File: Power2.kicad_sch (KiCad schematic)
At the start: 22 parts, among them U1001 AP64060QWU, U1002 AP7383, U1003 LM2776, U1004 XC6901D121MR-G

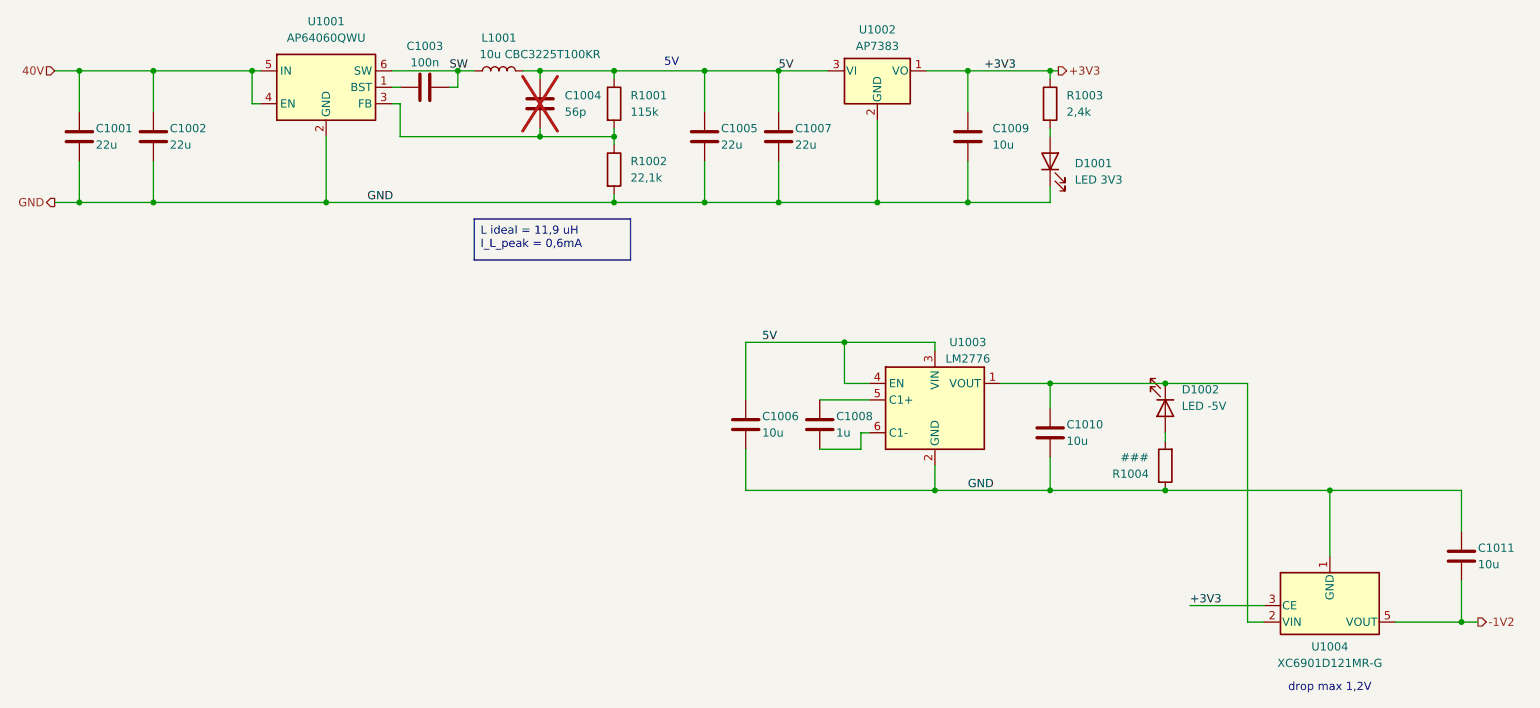
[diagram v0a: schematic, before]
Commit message: added Ch2 and removed global power flags
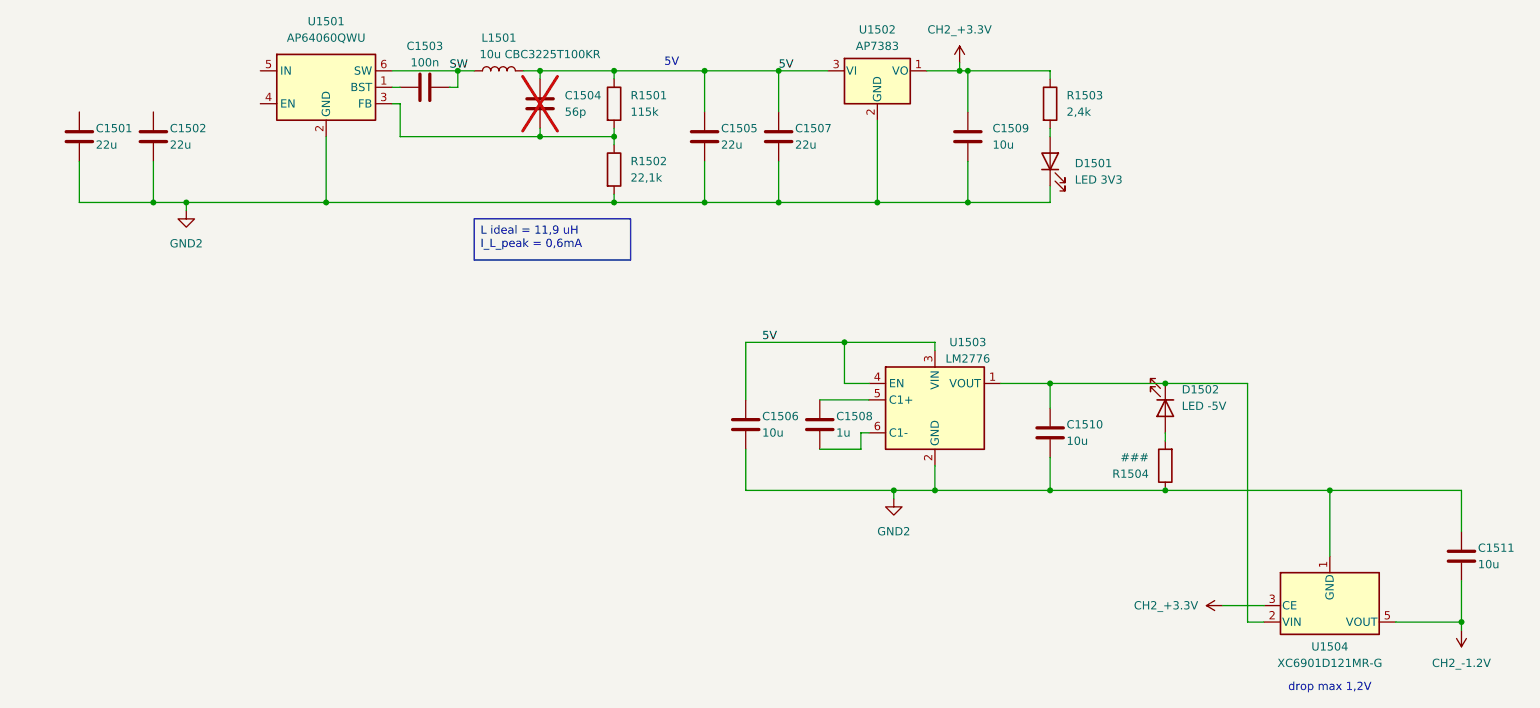
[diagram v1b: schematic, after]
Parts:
- removed C1001, C1002: 22u, Capacitor_SMD:C_1206_3216Metric, symbol Device:C
- removed C1003: 100n, Capacitor_SMD:C_0603_1608Metric, symbol Device:C
- removed C1004: 56p, Capacitor_SMD:C_0603_1608Metric, symbol Device:C
- removed C1005, C1007: 22u, Capacitor_SMD:C_0805_2012Metric, symbol Device:C
- removed C1006, C1009, C1010, C1011: 10u, Capacitor_SMD:C_0805_2012Metric, symbol Device:C
- removed C1008: 1u, Capacitor_SMD:C_0805_2012Metric, symbol Device:C
- removed D1001: LED 3V3, LED_SMD:LED_0603_1608Metric, symbol Device:LED
- removed D1002: LED -5V, LED_SMD:LED_0603_1608Metric, symbol Device:LED
- removed L1001: 10u CBC3225T100KR, Inductor_SMD:L_1210_3225Metric, symbol Device:L
- removed R1001: 115k, Resistor_SMD:R_0603_1608Metric, symbol Device:R
- removed R1002: 22,1k, Resistor_SMD:R_0603_1608Metric, symbol Device:R
- removed R1003: 2,4k, Resistor_SMD:R_0603_1608Metric, symbol Device:R
- removed R1004: ###, Resistor_SMD:R_0603_1608Metric, symbol Device:R
- removed U1001: AP64060QWU, Package_TO_SOT_SMD:TSOT-23-6, symbol Regulator_Switching:AP63200WU
- removed U1002: AP7383, Package_TO_SOT_SMD:SOT-89-3, symbol Regulator_Linear:AP7384-33Y
- removed U1003: LM2776, Package_TO_SOT_SMD:SOT-23-6, symbol Regulator_SwitchedCapacitor:LM2776
- removed U1004: XC6901D121MR-G, Package_TO_SOT_SMD:SC-74A-5_1.55x2.9mm_P0.95mm, symbol Regulator_Linear:LT1964-SD
- added C1501, C1502: 22u, Capacitor_SMD:C_1206_3216Metric, symbol Device:C
- added C1503: 100n, Capacitor_SMD:C_0603_1608Metric, symbol Device:C
- added C1504: 56p, Capacitor_SMD:C_0603_1608Metric, symbol Device:C
- added C1505, C1507: 22u, Capacitor_SMD:C_0805_2012Metric, symbol Device:C
- added C1506, C1509, C1510, C1511: 10u, Capacitor_SMD:C_0805_2012Metric, symbol Device:C
- added C1508: 1u, Capacitor_SMD:C_0805_2012Metric, symbol Device:C
- added D1501: LED 3V3, LED_SMD:LED_0603_1608Metric, symbol Device:LED
- added D1502: LED -5V, LED_SMD:LED_0603_1608Metric, symbol Device:LED
- added L1501: 10u CBC3225T100KR, Inductor_SMD:L_1210_3225Metric, symbol Device:L
- added R1501: 115k, Resistor_SMD:R_0603_1608Metric, symbol Device:R
- added R1502: 22,1k, Resistor_SMD:R_0603_1608Metric, symbol Device:R
- added R1503: 2,4k, Resistor_SMD:R_0603_1608Metric, symbol Device:R
- added R1504: ###, Resistor_SMD:R_0603_1608Metric, symbol Device:R
- added U1501: AP64060QWU, Package_TO_SOT_SMD:TSOT-23-6, symbol Regulator_Switching:AP63200WU
- added U1502: AP7383, Package_TO_SOT_SMD:SOT-89-3, symbol Regulator_Linear:AP7384-33Y
- added U1503: LM2776, Package_TO_SOT_SMD:SOT-23-6, symbol Regulator_SwitchedCapacitor:LM2776
- added U1504: XC6901D121MR-G, Package_TO_SOT_SMD:SC-74A-5_1.55x2.9mm_P0.95mm, symbol Regulator_Linear:LT1964-SD
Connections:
- net 5V: now also C1504.1, C1505.1, C1506.1, C1507.1, L1501.2, R1501.1, U1502.3 (VI), U1503.3 (VIN), U1503.4 (EN)
- net SW: now also C1503.2, L1501.1, U1501.6 (SW)
- new net: C1510.1, D1502.1 (K), U1503.1 (VOUT), U1504.2 (VIN)
- new net: D1502.2 (A), R1504.2
- new net: C1504.2, R1501.2, R1502.1, U1501.3 (FB)
- new net: C1508.1, U1503.5 (C1+)
- new net: C1508.2, U1503.6 (C1-)
- new net: D1501.2 (A), R1503.2
- new net: C1503.1, U1501.1 (BST)
- new net CH2_+3.3V: C1509.1, R1503.1, U1502.1 (VO), U1504.3 (CE)
- new net CH2_-1.2V: C1511.2, U1504.5 (VOUT)
- new net GND2: C1501.2, C1502.2, C1505.2, C1506.2, C1507.2, C1509.2, C1510.2, C1511.1, D1501.1 (K), R1502.2, R1504.1, U1501.2 (GND), U1502.2 (GND), U1503.2 (GND), U1504.1 (GND)
